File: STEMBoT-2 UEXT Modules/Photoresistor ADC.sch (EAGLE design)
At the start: 18 parts, among them IC1 74HC165PW,118, IC2 LMV324DR2G, IC3 LMV324DR2G, Q1 MMBT3904LP-7

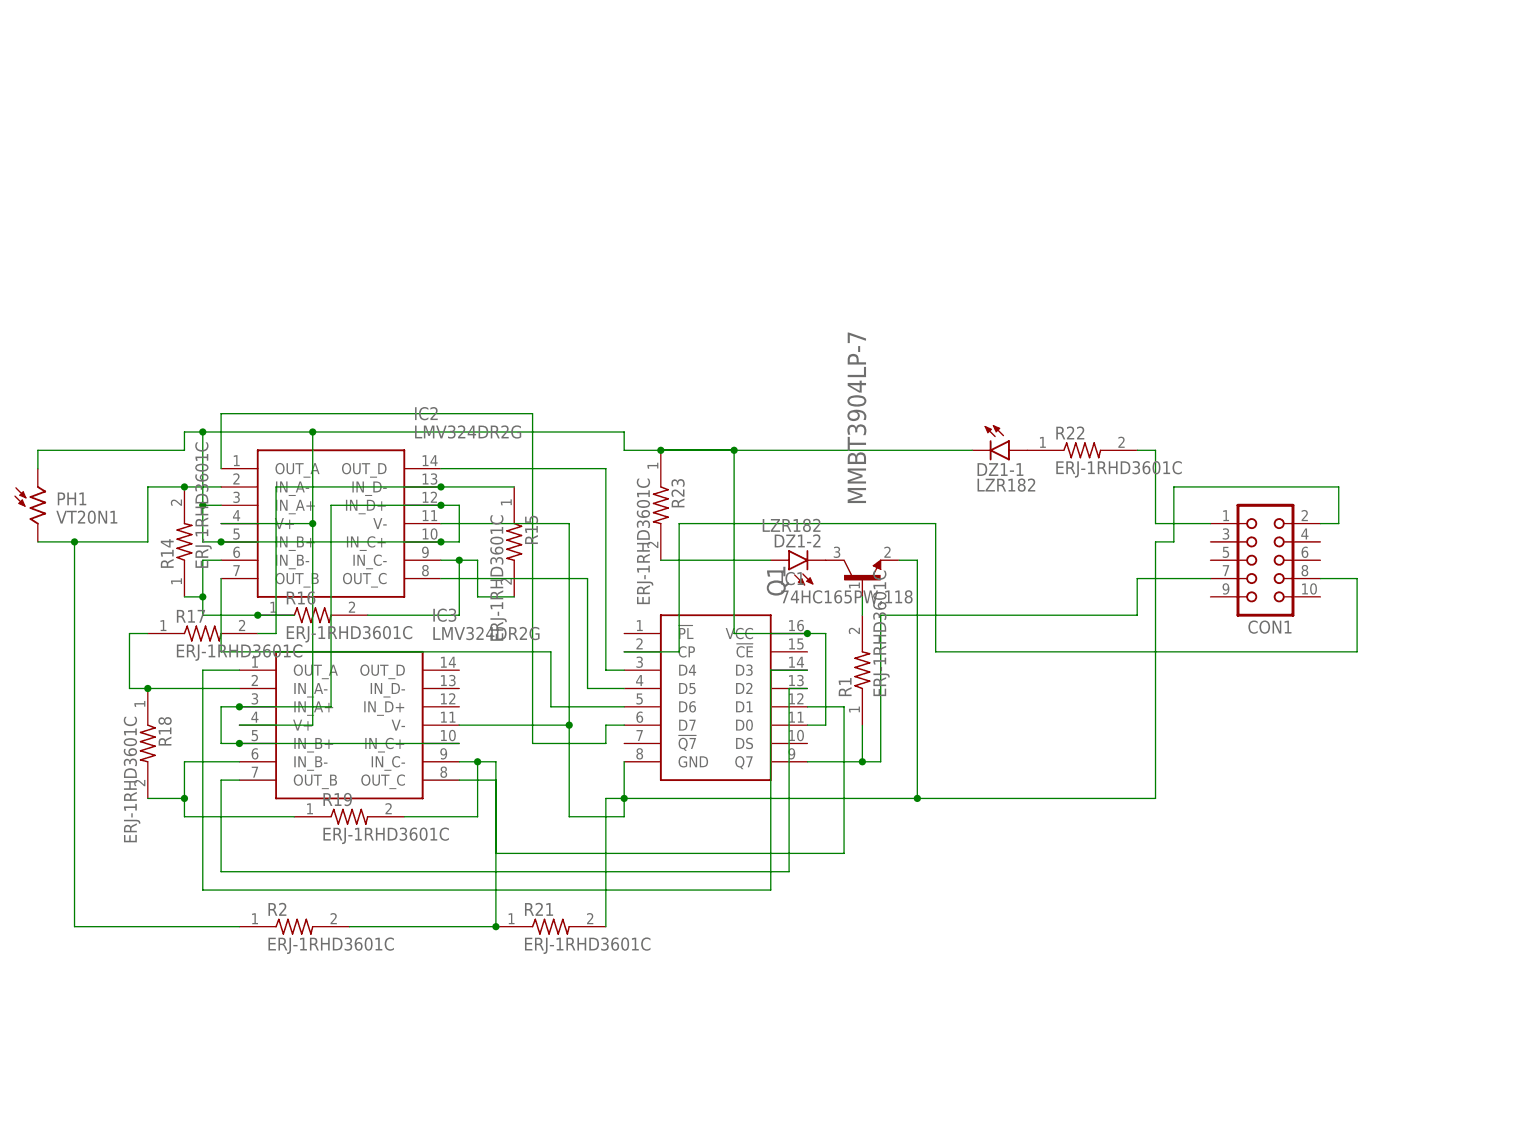
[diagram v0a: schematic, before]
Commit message: Adjusted ADC modules for PCB order. Dan, these are auto-routed.
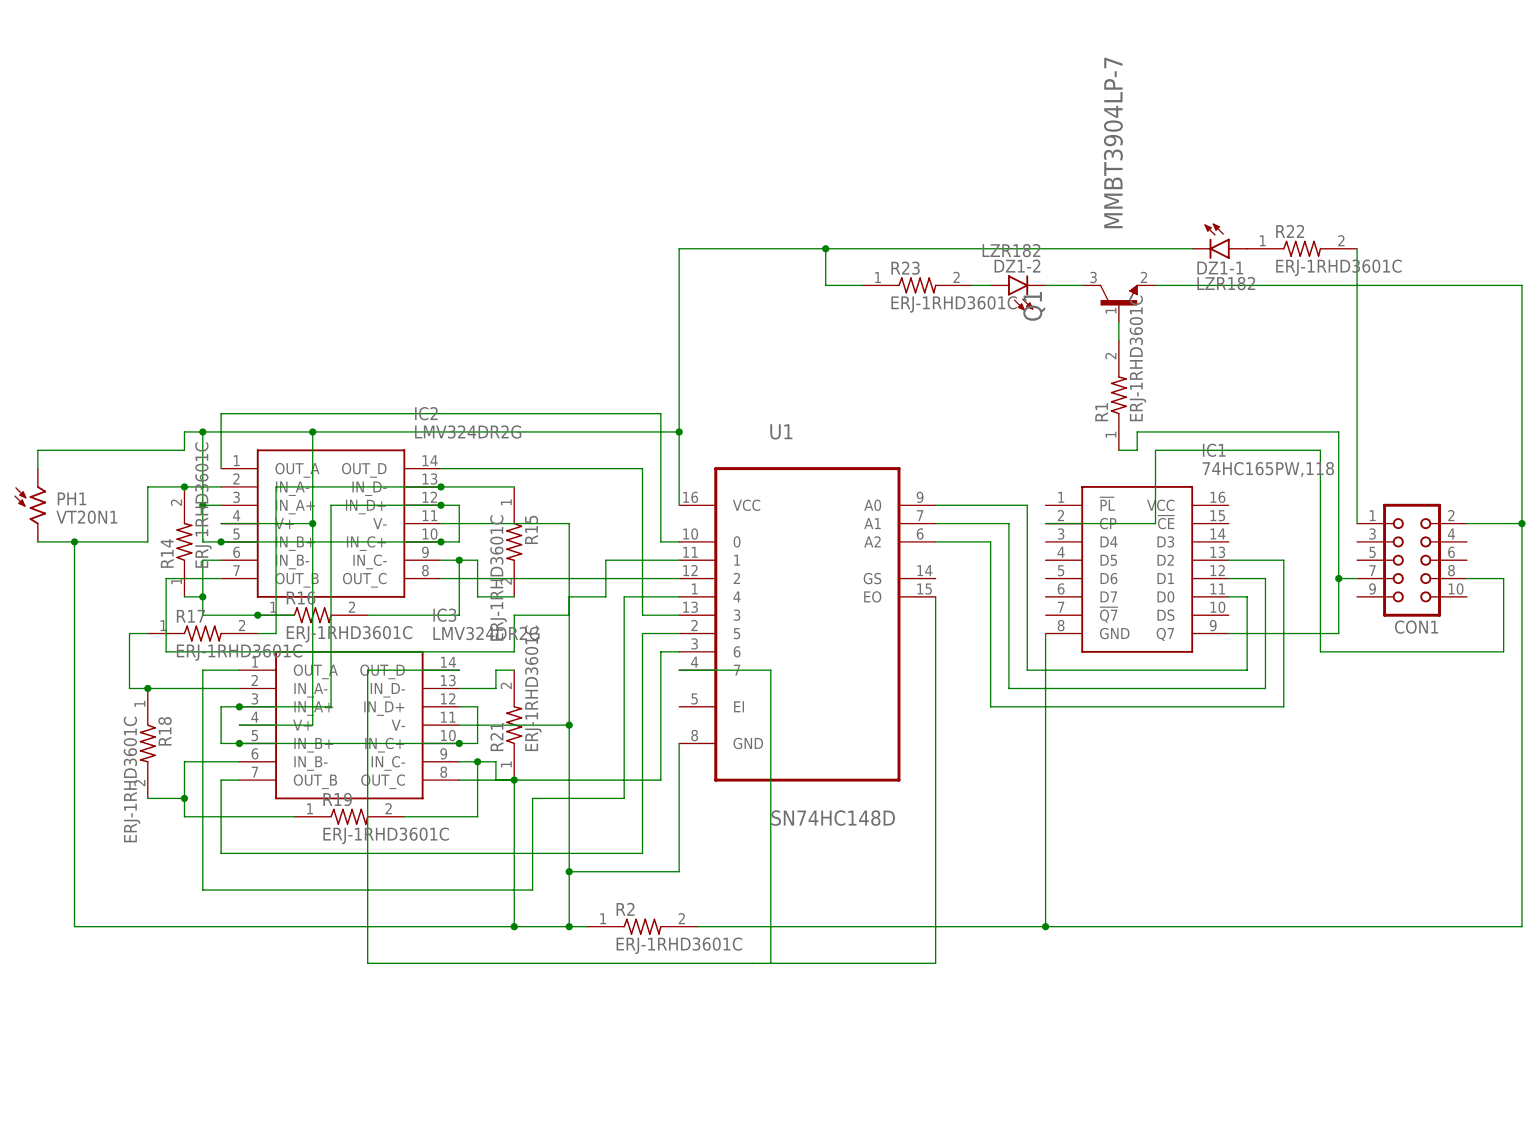
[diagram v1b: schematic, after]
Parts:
- added U1: SN74HC148D, SN74HC148D:SN74HC148D
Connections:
- removed net N$17: IC3.IN_C-, R19.2, R2.2, R21.1
- removed net N$32: IC1.D6, IC2.OUT_B
- removed net N$6 (its old number): IC1.D1, IC3.OUT_C
- removed net N$7 (its old number): DZ1-1.C, IC1.D0, IC1.VCC, IC2.IN_A+, IC2.IN_B+, IC2.IN_C+, IC2.IN_D+, IC2.V+, IC3.IN_A+, IC3.IN_B+, IC3.IN_C+, IC3.V+, PH1.1, R23.1
- new net N$12: DZ1-1.C, IC2.IN_A+, IC2.IN_B+, IC2.IN_C+, IC2.IN_D+, IC2.V+, IC3.IN_A+, IC3.IN_B+, IC3.IN_C+, IC3.IN_D+, IC3.V+, PH1.1, R23.1, U1.VCC
- new net N$15: IC3.IN_D-, R21.2
- new net N$16: IC3.OUT_D, U1.7, U1.EO
- new net N$19: IC1.D0, U1.A0
- new net N$20: IC1.D1, U1.A1
- new net N$21: IC1.D2, U1.A2
- new net N$22: CON1.2, IC1.GND, Q1.E, R2.2
- new net N$8: IC2.IN_A-, IC2.V-, IC3.IN_C-, IC3.V-, PH1.2, R14.2, R19.2, R2.1, R21.1, U1.GND
- net N$11: now also IC3.OUT_C, U1.6; no longer IC2.IN_A-, PH1.2, R14.2, R2.1
- net N$2: now also IC2.OUT_B, U1.1; no longer CON1.2, IC1.GND, IC2.V-, IC3.V-, Q1.E, R21.2
- net N$23: now also U1.5; no longer IC1.D2
- net N$26: now also U1.4; no longer IC1.D3
- net N$30: now also U1.3; no longer IC1.D4
- net N$31: now also U1.2; no longer IC1.D5
- net N$33: now also U1.0; no longer IC1.D7
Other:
- moved on the sheet: CON1, DZ1-1, DZ1-2, IC1, Q1, R1, R2, R21, R22, R23

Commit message: Once again, updating ADC shematics and boards. Used autorouter.
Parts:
- removed IC2, IC3: LMV324DR2G, LMV324DR2G:LMV324DR2G
- added R3: ERJ-1RHD3601C, Resistor:ERJ-1RHD3601C
- added U2, U3: MAX964ESET, MAX964ESET:MAX964ESET
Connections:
- removed net N$2: IC2.OUT_B, U1.1
- removed net N$30: IC2.OUT_D, U1.3
- removed net N$31: IC2.OUT_C, U1.2
- removed net N$33: IC2.OUT_A, U1.0
- new net N$17: U1.6, U2.QB
- new net N$18: U1.5, U2.QC
- new net N$27: U1.2, U3.QB
- new net N$28: U1.1, U3.QC
- new net N$29: U1.0, U3.QD
- net N$10: now also R17.2, U2.IND-; no longer IC2.IN_B-, R14.1
- net N$11: now also R17.1, R21.2, U3.INA-; no longer IC3.OUT_C, U1.6
- net N$12: now also R3.2, U2.GND, U2.VCC; no longer IC2.IN_A+, IC2.IN_B+, IC2.IN_C+, IC2.IN_D+, IC2.V+, IC3.IN_A+, IC3.IN_B+, IC3.IN_C+, IC3.IN_D+, IC3.V+
- net N$13: now also R18.1, R21.1, U3.INB-; no longer IC2.IN_C-, R15.2, R16.2
- net N$14: now also R18.2, R19.2, U3.INC-; no longer IC2.IN_D-, R15.1, R17.2
- net N$15: now also PH1.2, R19.1, R2.1, U2.INA+, U2.INB+, U2.INC+, U2.IND+, U3.GND, U3.INA+, U3.INB+, U3.INC+, U3.IND+, U3.IND-; no longer IC3.IN_D-, R21.2
- net N$16: now also U2.QA; no longer IC3.OUT_D, U1.EO
- net N$22: now also U1.GND
- net N$23: now also U1.3, U2.QD; no longer IC3.OUT_B, U1.5
- net N$26: now also U3.QA; no longer IC3.OUT_A
- net N$3: now also R15.2, R16.2, U2.INC-; no longer IC3.IN_A-, R17.1, R18.1
- net N$8: now also R3.1, U2.INA-; no longer IC2.IN_A-, IC2.V-, IC3.IN_C-, IC3.V-, PH1.2, R19.2, R2.1, R21.1, U1.GND
- net N$9: now also R14.1, R15.1, U2.INB-; no longer IC3.IN_B-, R18.2, R19.1
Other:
- moved on the sheet: R14, R15, R16, R17, R18, R19, R21
